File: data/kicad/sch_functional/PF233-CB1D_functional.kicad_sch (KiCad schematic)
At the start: 61 parts, among them M5 5 V 1.5 A switching module, U1 Pico 2 W

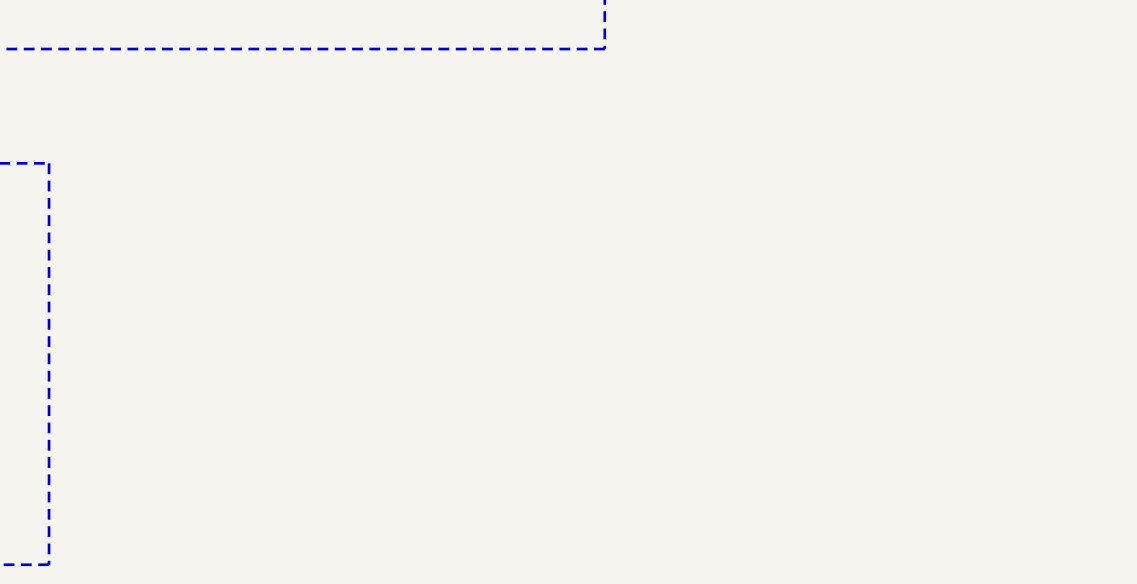
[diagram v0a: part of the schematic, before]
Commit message: WIP stage 5: B3/B5/B6/B8 closed in blockers.json, B7 narrowed to HVTERM, B12 opened; cap-v18 pipeline step (cap was not regenerated on a fresh work/); upper_check septum joint by voxels; curated STLs refreshed (U6 dock for the real MT60, septum lap segments, canonical face order); DESIGN_STATE stress counts
Co-Authored-By: Claude Opus 5.5 <noreply@anthropic.com>
Claude-Session: https://claude.ai/code/session_01FX4DWSYYjMCFGGA6gmha65
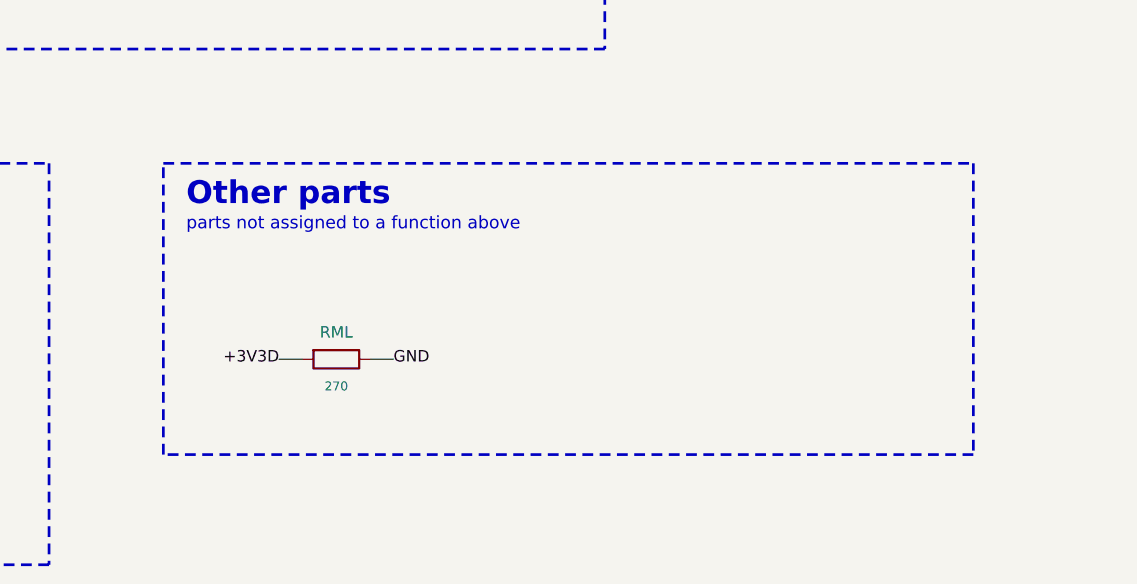
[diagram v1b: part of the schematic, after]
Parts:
- added RML: 270, Resistor_SMD:R_0603_1608Metric, symbol PF233F:R_H
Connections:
- net +3V3D: now also RML.1
- net GND: now also RML.2
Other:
- note added: "Other parts"
- note added: "parts not assigned to a function above"
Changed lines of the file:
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@@
   (wire (pts (xy 49.530 426.720) (xy 52.070 426.720)) (stroke (width 0) (type default)))
   (label "GND" (at 52.070 426.720 0) (fields_autoplaced yes) (effects (font (size 1.27 1.27)) (justify left)))
+  (rectangle (start 123.02 397.33) (end 213.02 429.69) (stroke (width 0.3) (type dash)) (fill (type none)))
+  (text "Other parts" (exclude_from_sim no) (at 125.560 399.330 0) (effects (font (size 2.54 2.54) bold) (justify left top)))
+  (text "parts not assigned to a function above" (exclude_from_sim no) (at 125.560 403.330 0) (effects (font (size 1.4 1.4)) (justify left top)))
+  (symbol (lib_id "PF233F:R_H") (at 142.240 419.100 0) (unit 1) (exclude_from_sim no) (in_bom yes) (on_board yes) (dnp no)
+    (property "Reference" "RML" (at 142.240 416.100 0) (effects (font (size 1.27 1.27))))
+    (property "Value" "270" (at 142.240 422.100 0) (effects (font (size 1.0 1.0))))
+    (property "Footprint" "Resistor_SMD:R_0603_1608Metric" (at 142.240 419.100 0) (effects (font (size 1.27 1.27)) hide))
+    (pin "1")
+    (pin "2")
+    (instances (project "PF233-CB1D" (path "/510629a9-bbcb-5470-879a-e8d7a5640f55" (reference "RML") (unit 1))))
+  )
+  (wire (pts (xy 138.430 419.100) (xy 135.890 419.100)) (stroke (width 0) (type default)))
+  (label "+3V3D" (at 135.890 419.100 180) (fields_autoplaced yes) (effects (font (size 1.27 1.27)) (justify right)))
+  (wire (pts (xy 146.050 419.100) (xy 148.590 419.100)) (stroke (width 0) (type default)))
+  (label "GND" (at 148.590 419.100 0) (fields_autoplaced yes) (effects (font (size 1.27 1.27)) (justify left)))
   (sheet_instances (path "/" (page "1")))
 )

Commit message: WIP: sign-off re-run outputs (publish in progress)
Co-Authored-By: Claude Opus 5.5 <noreply@anthropic.com>
Claude-Session: https://claude.ai/code/session_01FX4DWSYYjMCFGGA6gmha65
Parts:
- JLB: value to LB1: +5V, LED_IN, GND, GND -> to LB1: +5V, LED_IN, LED_CLK, GND
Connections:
- net GND: no longer JLB.3
- net LED_CLK: now reaches U1.19 (GP14)
- net LED_CLK: now also JLB.3
- no-connect marks 10 -> 9
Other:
- note added: "JLB: +5V, LED_IN, LED_CLK (from the Pico), GND to LB1."
- note added: "PF233-CB1D: CB1D-C1 controller: Pico 2 W, supplies, handle cable, receive-board links, TX monitor"
- note removed: "JLB: +5V, LED_IN (from the Pico), GND, GND to LB1."
- note removed: "PF233-CB1D: CB1D-B controller: Pico 2 W, supplies, handle cable, receive-board links, TX monitor"
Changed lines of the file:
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@@
 (kicad_sch (version 20231120) (generator "arx_sch_func") (generator_version "1") (paper "User" 609.6 508.0)
-  (title_block (title "PF233-CB1D  functional schematic") (date "2026-10-26") (rev "r3") (company "ARX / PHI-FOLD 233") (comment 1 "CB1D-B controller: Pico 2 W, supplies, handle cable, receive-board links, TX monitor") (comment 2 "MODELED design: not built, not bench-tested.") (comment 3 "Generated: src/pcb/sch_func.py; checked against the netlist."))
+  (title_block (title "PF233-CB1D  functional schematic") (date "2026-10-26") (rev "r3") (company "ARX / PHI-FOLD 233") (comment 1 "CB1D-C1 controller: Pico 2 W, supplies, handle cable, receive-board links, TX monitor") (comment 2 "MODELED design: not built, not bench-tested.") (comment 3 "Generated: src/pcb/sch_func.py; checked against the netlist."))
   (text "How to read: parts sit in functional blocks (dashed frames). Every pin ends in a short wire with its NET NAME; equal names are connected (also between blocks). A cross = intentionally unconnected pin." (exclude_from_sim no) (at 20.320 10.160 0) (effects (font (size 1.4 1.4)) (justify left top)))
   (text "Diode symbols point anode to cathode. Pin names are those of the library; items marked VERIFY in docs/ASSUMPTIONS.md are unverified. MODELED design: not built, not bench-tested." (exclude_from_sim no) (at 20.320 14.000 0) (effects (font (size 1.4 1.4)) (justify left top)))
-  (text "PF233-CB1D: CB1D-B controller: Pico 2 W, supplies, handle cable, receive-board links, TX monitor" (exclude_from_sim no) (at 20.320 4.000 0) (effects (font (size 2.5 2.5) bold) (justify left top)))
+  (text "PF233-CB1D: CB1D-C1 controller: Pico 2 W, supplies, handle cable, receive-board links, TX monitor" (exclude_from_sim no) (at 20.320 4.000 0) (effects (font (size 2.5 2.5) bold) (justify left top)))
   (rectangle (start 20.32 38.10) (end 183.68 126.54) (stroke (width 0.3) (type dash)) (fill (type none)))
   (text "1  Controller" (exclude_from_sim no) (at 22.860 40.100 0) (effects (font (size 2.54 2.54) bold) (justify left top)))
@@
   (label "GND" (at 38.100 105.410 180) (fields_autoplaced yes) (effects (font (size 1.27 1.27)) (justify right)))
   (wire (pts (xy 40.640 107.950) (xy 38.100 107.950)) (stroke (width 0) (type default)))
-  (no_connect (at 38.100 107.950))
+  (label "LED_CLK" (at 38.100 107.950 180) (fields_autoplaced yes) (effects (font (size 1.27 1.27)) (justify right)))
   (wire (pts (xy 40.640 110.490) (xy 38.100 110.490)) (stroke (width 0) (type default)))
   (no_connect (at 38.100 110.490))
@@
   (rectangle (start 20.32 397.33) (end 110.32 441.93) (stroke (width 0.3) (type dash)) (fill (type none)))
   (text "13  Display link" (exclude_from_sim no) (at 22.860 399.330 0) (effects (font (size 2.54 2.54) bold) (justify left top)))
-  (text "JLB: +5V, LED_IN (from the Pico), GND, GND to LB1." (exclude_from_sim no) (at 22.860 403.330 0) (effects (font (size 1.4 1.4)) (justify left top)))
+  (text "JLB: +5V, LED_IN, LED_CLK (from the Pico), GND to LB1." (exclude_from_sim no) (at 22.860 403.330 0) (effects (font (size 1.4 1.4)) (justify left top)))
   (symbol (lib_id "PF233F:BOX_HDR1x4") (at 39.370 425.450 0) (unit 1) (exclude_from_sim no) (in_bom yes) (on_board yes) (dnp no)
     (property "Reference" "JLB" (at 39.370 415.110 0) (effects (font (size 1.27 1.27))))
-    (property "Value" "to LB1: +5V, LED_IN, GND, GND" (at 39.370 435.350 0) (effects (font (size 1.0 1.0))))
+    (property "Value" "to LB1: +5V, LED_IN, LED_CLK, GND" (at 39.370 435.350 0) (effects (font (size 1.0 1.0))))
     (property "Footprint" "Connector:Pin_header_1x4_P2.54mm" (at 39.370 425.450 0) (effects (font (size 1.27 1.27)) hide))
     (pin "1")
@@
   (label "LED_IN" (at 52.070 421.640 0) (fields_autoplaced yes) (effects (font (size 1.27 1.27)) (justify left)))
   (wire (pts (xy 49.530 424.180) (xy 52.070 424.180)) (stroke (width 0) (type default)))
-  (label "GND" (at 52.070 424.180 0) (fields_autoplaced yes) (effects (font (size 1.27 1.27)) (justify left)))
+  (label "LED_CLK" (at 52.070 424.180 0) (fields_autoplaced yes) (effects (font (size 1.27 1.27)) (justify left)))
   (wire (pts (xy 49.530 426.720) (xy 52.070 426.720)) (stroke (width 0) (type default)))
   (label "GND" (at 52.070 426.720 0) (fields_autoplaced yes) (effects (font (size 1.27 1.27)) (justify left)))

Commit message: WIP: CB1D-C2 dual-source gyro land (BMI270 / LSM6DSO, pins 2-3 to VDDIO), LSM6DSO datasheet logged, gyro cluster re-placed for escape; CB1D re-route running
Co-Authored-By: Claude Opus 5.5 <noreply@anthropic.com>
Claude-Session: https://claude.ai/code/session_01FX4DWSYYjMCFGGA6gmha65
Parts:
- added CG1, CG2: 100n, Capacitor_SMD:C_0603_1608Metric, symbol PF233F:C_H
- added RGA, RGL: 4k7, Resistor_SMD:R_0603_1608Metric, symbol PF233F:R_H
- added UG: BMI270, PF233:BMI270_LGA-14_2.5x3.0mm, symbol PF233F:BOX_BMI270
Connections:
- net GND: now also CG1.2, CG2.2, UG.1 (SDO), UG.6 (GNDIO), UG.7 (GND)
- net P3V3: now also CG1.1, CG2.1, RGA.1, RGL.1, UG.12 (CSB), UG.5 (VDDIO), UG.8 (VDD)
- net GYR_SDA: now reaches U1.21 (GP16)
- net GYR_SDA: now also RGA.2, UG.14 (SDX)
- net GYR_SCL: now reaches U1.22 (GP17)
- net GYR_SCL: now also RGL.2, UG.13 (SCX)
- no-connect marks 9 -> 13
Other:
- note added: "14 Yaw gyro (sweep direction)"
- note added: "PF233-CB1D: CB1D-C2 controller: Pico 2 W, supplies, handle cable, receive-board links, TX monitor"
- note added: "RGA / RGL 4k7 pull-ups. Read in the idle slot after the receive window."
- note added: "UG BMI270 on I2C (Pico pins 21 / 22): SDO to GND (default address), CSB to P3V3; CG1 / CG2 100 nF at VDDIO / VDD;"
- note added: "UG_ASCX_NC"
- note added: "UG_ASDX_NC"
- note added: "UG_INT1_NC"
- note added: "UG_INT2_NC"
- note added: "UG_OCSB_NC"
- note added: "UG_OSDO_NC"
- note removed: "PF233-CB1D: CB1D-C1 controller: Pico 2 W, supplies, handle cable, receive-board links, TX monitor"
- moved on the sheet: RML

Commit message: WIP (NOT signed off): data published by the first close-out sign-off run, which had 5 FAIL (CB1D-C2 / AU1 fine-pitch clearance); superseded by the rerun in progress
Co-Authored-By: Claude Opus 5.5 <noreply@anthropic.com>
Claude-Session: https://claude.ai/code/session_01FX4DWSYYjMCFGGA6gmha65
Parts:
- removed RJ5: 0R DNP, Resistor_SMD:R_0603_1608Metric, symbol PF233F:R_H
- added DAU1, DAU2: BAS16, Diode_SMD:D_SOD-123, symbol PF233F:D_H
- added RAU: 100R, Resistor_SMD:R_0603_1608Metric, symbol PF233F:R_H
- added RGF: 10R, Resistor_SMD:R_0603_1608Metric, symbol PF233F:R_H
- JTR: value Handle: +3V3 GND TRIG DIAL JOYX JOYY SHLD -> Handle: +3V3 GND TRIG DIAL AUD_LINK - SHLD
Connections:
- net GND: now also DAU2.2; no longer UG.1 (SDO)
- net GYR_SCL: now also U1.27 (GP21); no longer U1.22 (GP17)
- net GYR_SDA: now also U1.26 (GP20); no longer U1.21 (GP16)
- net P3V3: now also DAU1.1, RGF.1; no longer CG1.1, CG2.1, UG.12 (CSB), UG.5 (VDDIO), UG.8 (VDD)
- net AUD_PIO: now reaches U1.20 (GP15)
- net AUD_PIO: now also RAU.2
- net UG_VIO: now reaches UG.2 (ASDX)
- net UG_VIO: now also CG1.1, CG2.1, UG.1 (SDO), UG.12 (CSB), UG.3 (ASCX), UG.5 (VDDIO), UG.8 (VDD), RGF.2
- net JTR5_OPT renamed AUD_LINK
- net AUD_LINK: now also DAU1.2, DAU2.1, RAU.1
- no-connect marks 13 -> 10
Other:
- note added: "8 Handle cable: trigger, dial, audio link, shield"
- note added: "AUD_LINK (CB1D-C2): half-duplex link to AU1 from Pico pin 20 through RAU 100 R, BAS16 clamps DAU1 / DAU2. RJ6 (0 R, not fitted): optional grounding of JTR.6. RSH + CSH shield termination."
- note added: "JTR: +3V3, GND, TRIG, DIAL, AUD_LINK, -, SHLD (the only signal cable leaving the head)."
- note added: "UG BMI270 (alternate: ST LSM6DSO, same land) on I2C (Pico pins 26 / 27, alternate address: SDO high); UG_VIO = VDD, VDDIO, CSB, SDO, pins 2 / 3,"
- note added: "fed from P3V3 by RGF 10 R with CG1 / CG2 100 nF; RGA / RGL 4k7 pull-ups. Read in the idle slot after the receive window."
- note removed: "8 Handle cable: trigger, dial, shield"
- note removed: "JTR: +3V3, GND, TRIG, DIAL, JOYX, JOYY, SHLD (the only signal cable leaving the head)."
- note removed: "RGA / RGL 4k7 pull-ups. Read in the idle slot after the receive window."
- note removed: "RJ5 / RJ6 (0 R, not fitted): optional grounding of JTR.5 / JTR.6. RSH + CSH shield termination."
- note removed: "UG BMI270 on I2C (Pico pins 21 / 22): SDO to GND (default address), CSB to P3V3; CG1 / CG2 100 nF at VDDIO / VDD;"
- note removed: "UG_ASCX_NC"
- note removed: "UG_ASDX_NC"
- moved on the sheet: CG1, CG2, CHTA, CSH, CUS, DHA1, DHA2, JA, JB, JCL, JHTA, JLB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

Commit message: WIP (NOT signed off): data published by the second close-out run (8 FAIL: 3 opens on CB1D-C2 / AU1 under the exact fine-zone keep-out); third run in progress
Co-Authored-By: Claude Opus 5.5 <noreply@anthropic.com>
Claude-Session: https://claude.ai/code/session_01FX4DWSYYjMCFGGA6gmha65
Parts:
- JCL: value Coil leads from the neck module: COIL_B (dra -> Coil taps from TXJ1: COIL_B (drain side), CO; footprint Connector:Terminal_block_1x2_P5.08mm -> Connector:Solder_holes_AWG22_1x2_P5.08mm; symbol PF233F:BOX_TERM2 -> PF233F:BOX_WIRE2_AWG22
- JDBG: symbol PF233F:BOX_HDR1x2 -> PF233F:BOX_WIRE1x2
- JLB: footprint Connector:Pin_header_1x4_P2.54mm -> Connector:Wire_pads_1x4_P2.54mm; symbol PF233F:BOX_HDR1x4 -> PF233F:BOX_WIRE1x4
- JPB: symbol PF233F:BOX_HDR2x4 -> PF233F:BOX_WIRE2x4
- JPW: symbol PF233F:BOX_TERM4 -> PF233F:BOX_WIRE4T
- JTR: symbol PF233F:BOX_HDR1x7 -> PF233F:BOX_WIRE1x7
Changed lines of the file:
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@@
   (wire (pts (xy 66.040 110.490) (xy 68.580 110.490)) (stroke (width 0) (type default)))
   (no_connect (at 68.580 110.490))
-  (symbol (lib_id "PF233F:BOX_HDR1x2") (at 104.140 66.040 0) (unit 1) (exclude_from_sim no) (in_bom yes) (on_board yes) (dnp no)
+  (symbol (lib_id "PF233F:BOX_WIRE1x2") (at 104.140 66.040 0) (unit 1) (exclude_from_sim no) (in_bom yes) (on_board yes) (dnp no)
     (property "Reference" "JDBG" (at 104.140 59.080 0) (effects (font (size 1.27 1.27))))
     (property "Value" "RUN / GND (reset, SWD pads on Pico underside" (at 104.140 74.240 0) (effects (font (size 1.0 1.0))))
@@
   (text "2  Power input and protection" (exclude_from_sim no) (at 198.920 40.100 0) (effects (font (size 2.54 2.54) bold) (justify left top)))
   (text "JPW: VBUS x2 / GND x2 from the shaft -> F1 5 A slow-blow -> VBUS (DTV: 30 V TVS, CI1 / CI2 10 uF bulk)." (exclude_from_sim no) (at 198.920 44.100 0) (effects (font (size 1.4 1.4)) (justify left top)))
-  (symbol (lib_id "PF233F:BOX_TERM4") (at 215.900 66.040 0) (unit 1) (exclude_from_sim no) (in_bom yes) (on_board yes) (dnp no)
+  (symbol (lib_id "PF233F:BOX_WIRE4T") (at 215.900 66.040 0) (unit 1) (exclude_from_sim no) (in_bom yes) (on_board yes) (dnp no)
     (property "Reference" "JPW" (at 215.900 55.880 0) (effects (font (size 1.27 1.27))))
     (property "Value" "Power in: VBUS VBUS GND GND (from shaft)" (at 215.900 76.120 0) (effects (font (size 1.0 1.0))))
@@
   (text "TRIG / DIAL inputs: series 1 k, BAS16 clamps to P3V3 / GND (DH / DL), 10 nF, pull-ups RP1 47 k / RP2 10 k." (exclude_from_sim no) (at 149.980 240.010 0) (effects (font (size 1.4 1.4)) (justify left top)))
   (text "AUD_LINK (CB1D-C2): half-duplex link to AU1 from Pico pin 20 through RAU 100 R, BAS16 clamps DAU1 / DAU2. RJ6 (0 R, not fitted): optional grounding of JTR.6. RSH + CSH shield termination." (exclude_from_sim no) (at 149.980 243.210 0) (effects (font (size 1.4 1.4)) (justify left top)))
-  (symbol (lib_id "PF233F:BOX_HDR1x7") (at 166.370 267.970 0) (unit 1) (exclude_from_sim no) (in_bom yes) (on_board yes) (dnp no)
+  (symbol (lib_id "PF233F:BOX_WIRE1x7") (at 166.370 267.970 0) (unit 1) (exclude_from_sim no) (in_bom yes) (on_board yes) (dnp no)
     (property "Reference" "JTR" (at 166.370 254.990 0) (effects (font (size 1.27 1.27))))
     (property "Value" "Handle: +3V3 GND TRIG DIAL AUD_LINK - SHLD" (at 166.370 280.310 0) (effects (font (size 1.0 1.0))))
@@
   (text "JPB: 12V-side signals only: UMB_SHLD, TX1_IN, REF_I1, FAULT1_N, ISENSE1, NTC_SENSE, GND (same order as JC on PB1R)." (exclude_from_sim no) (at 22.860 346.210 0) (effects (font (size 1.4 1.4)) (justify left top)))
   (text "RUS / CUS bleed the umbilical shield." (exclude_from_sim no) (at 22.860 349.410 0) (effects (font (size 1.4 1.4)) (justify left top)))
-  (symbol (lib_id "PF233F:BOX_HDR2x4") (at 39.370 375.920 0) (unit 1) (exclude_from_sim no) (in_bom yes) (on_board yes) (dnp no)
+  (symbol (lib_id "PF233F:BOX_WIRE2x4") (at 39.370 375.920 0) (unit 1) (exclude_from_sim no) (in_bom yes) (on_board yes) (dnp no)
     (property "Reference" "JPB" (at 39.370 361.190 0) (effects (font (size 1.27 1.27))))
     (property "Value" "to PB1R: 12V GND TX1_IN REF_I1 FAULT1_N ISEN" (at 39.370 391.590 0) (effects (font (size 1.0 1.0))))
@@
   (text "JCL: coil leads COIL_B (drain side) / COIL_A (VBUS side). RDM1..3 (3 x 110 R, 600 V) form the damping chain DM1 / DM2 between them." (exclude_from_sim no) (at 187.310 346.210 0) (effects (font (size 1.4 1.4)) (justify left top)))
   (text "High-voltage nets COIL_B / DM1 / DM2: 1.0 mm rule." (exclude_from_sim no) (at 187.310 349.410 0) (effects (font (size 1.4 1.4)) (justify left top)))
-  (symbol (lib_id "PF233F:BOX_TERM2") (at 203.200 368.300 0) (unit 1) (exclude_from_sim no) (in_bom yes) (on_board yes) (dnp no)
+  (symbol (lib_id "PF233F:BOX_WIRE2_AWG22") (at 203.200 368.300 0) (unit 1) (exclude_from_sim no) (in_bom yes) (on_board yes) (dnp no)
     (property "Reference" "JCL" (at 203.200 361.190 0) (effects (font (size 1.27 1.27))))
-    (property "Value" "Coil leads from the neck module: COIL_B (dra" (at 203.200 376.350 0) (effects (font (size 1.0 1.0))))
-    (property "Footprint" "Connector:Terminal_block_1x2_P5.08mm" (at 203.200 368.300 0) (effects (font (size 1.27 1.27)) hide))
+    (property "Value" "Coil taps from TXJ1: COIL_B (drain side), CO" (at 203.200 376.350 0) (effects (font (size 1.0 1.0))))
+    (property "Footprint" "Connector:Solder_holes_AWG22_1x2_P5.08mm" (at 203.200 368.300 0) (effects (font (size 1.27 1.27)) hide))
     (pin "1")
     (pin "2")
@@
   (text "13  Display link" (exclude_from_sim no) (at 22.860 412.870 0) (effects (font (size 2.54 2.54) bold) (justify left top)))
   (text "JLB: +5V, LED_IN, LED_CLK (from the Pico), GND to LB1." (exclude_from_sim no) (at 22.860 416.870 0) (effects (font (size 1.4 1.4)) (justify left top)))
-  (symbol (lib_id "PF233F:BOX_HDR1x4") (at 39.370 438.150 0) (unit 1) (exclude_from_sim no) (in_bom yes) (on_board yes) (dnp no)
+  (symbol (lib_id "PF233F:BOX_WIRE1x4") (at 39.370 438.150 0) (unit 1) (exclude_from_sim no) (in_bom yes) (on_board yes) (dnp no)
     (property "Reference" "JLB" (at 39.370 428.650 0) (effects (font (size 1.27 1.27))))
     (property "Value" "to LB1: +5V, LED_IN, LED_CLK, GND" (at 39.370 448.890 0) (effects (font (size 1.0 1.0))))
-    (property "Footprint" "Connector:Pin_header_1x4_P2.54mm" (at 39.370 438.150 0) (effects (font (size 1.27 1.27)) hide))
-    (pin "1")
-    (pin "2")
+    (property "Footprint" "Connector:Wire_pads_1x4_P2.54mm" (at 39.370 438.150 0) (effects (font (size 1.27 1.27)) hide))
+    (pin "1")
+    (pin "2")

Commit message: WIP (NOT signed off): sign-off outputs with AU1 38 / 38 (exact DRC 0 / 0, all AU1 checks pass); CB1D 45 / 46 (TRIG_EXT open on the 0.125 grid, being re-routed on 0.15)
Co-Authored-By: Claude Opus 5.5 <noreply@anthropic.com>
Claude-Session: https://claude.ai/code/session_01FX4DWSYYjMCFGGA6gmha65
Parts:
- removed CG1, CG2: 100n, Capacitor_SMD:C_0603_1608Metric, symbol PF233F:C_H
- removed RGA, RGL: 4k7, Resistor_SMD:R_0603_1608Metric, symbol PF233F:R_H
- removed RGF: 10R, Resistor_SMD:R_0603_1608Metric, symbol PF233F:R_H
- removed UG: BMI270, PF233:BMI270_LGA-14_2.5x3.0mm, symbol PF233F:BOX_BMI270
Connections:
- net GYR_SCL: no longer names the net of U1.27 (GP21)
- net GYR_SDA: no longer names the net of U1.26 (GP20)
- no-connect marks 10 -> 8
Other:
- note added: "PF233-CB1D: CB1D-C2 controller: Pico 2 W, supplies, handle cable with the AU1 audio link, receive-board links, TX monitor"
- note removed: "14 Yaw gyro (sweep direction)"
- note removed: "PF233-CB1D: CB1D-C2 controller: Pico 2 W, supplies, handle cable, receive-board links, TX monitor"
- note removed: "UG BMI270 (alternate: ST LSM6DSO, same land) on I2C (Pico pins 26 / 27, alternate address: SDO high); UG_VIO = VDD, VDDIO, CSB, SDO, pins 2 / 3,"
- note removed: "UG_INT1_NC"
- note removed: "UG_INT2_NC"
- note removed: "UG_OCSB_NC"
- note removed: "UG_OSDO_NC"
- note removed: "fed from P3V3 by RGF 10 R with CG1 / CG2 100 nF; RGA / RGL 4k7 pull-ups. Read in the idle slot after the receive window."
- moved on the sheet: RML
